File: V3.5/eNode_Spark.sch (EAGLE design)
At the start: 80 parts, among them Q1 MOSFET-PCHANNEL_SOT23-3, U1 WM-N-BM-09, U10 OPA344, U2 MCP73831T-2ACI/OT, U3 R8008-33, U5 HTU21DSMD, U6 TMP006, U7 BMP180, U8 USD-SOCKETSMD, U9 MIC9.7MM

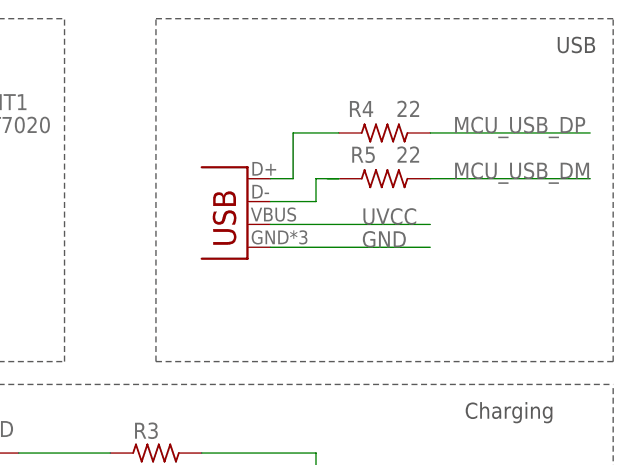
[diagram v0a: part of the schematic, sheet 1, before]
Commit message: Changed to Micro USB B.lbr
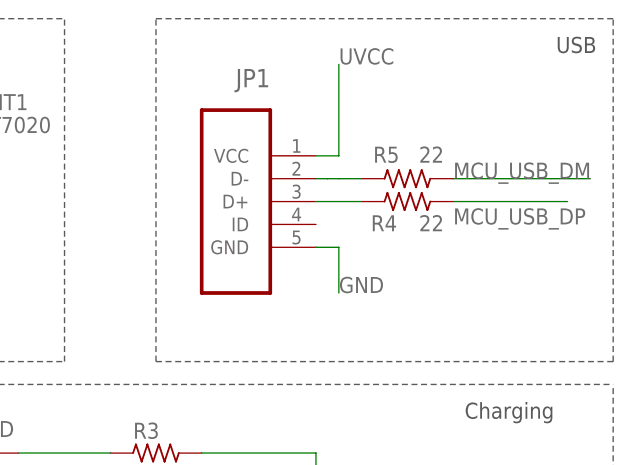
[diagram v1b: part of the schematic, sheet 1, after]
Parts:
- JP1: value USBUSB-MICROB-SLOT-HOLE -> (none); device Spark:USBUSB-MICROB-SLOT-HOLE -> Micro USB B:47346-0001
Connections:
- net MF renamed N$17
- net UVCC: now also JP1.VCC; no longer JP1.VBUS
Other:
- moved on the sheet: R4, R5
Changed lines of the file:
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@@
 <part name="+3V21" library="supply1" deviceset="+3V3" device=""/>
 <part name="R20" library="rc-master-smd" deviceset="R_" device="0603" value="2K"/>
-<part name="JP1" library="Spark" deviceset="USB" device="USB-MICROB-SLOT-HOLE"/>
+<part name="JP1" library="Micro USB B" deviceset="47346-0001" device=""/>
 </parts>
 <sheets>
@@
 <instance part="SW" gate="G$1" x="167.64" y="50.8" rot="MR0"/>
 <instance part="U$5" gate="G$1" x="0" y="0"/>
-<instance part="R4" gate="G$1" x="231.14" y="154.94" smashed="yes" rot="R180">
-<attribute name="NAME" x="227.076" y="156.718" size="1.778" layer="95"/>
-<attribute name="VALUE" x="232.41" y="156.718" size="1.778" layer="96"/>
-</instance>
-<instance part="R5" gate="G$1" x="231.14" y="149.86" smashed="yes" rot="R180">
-<attribute name="NAME" x="227.33" y="151.638" size="1.778" layer="95"/>
-<attribute name="VALUE" x="232.41" y="151.638" size="1.778" layer="96"/>
+<instance part="R4" gate="G$1" x="233.68" y="147.32" smashed="yes" rot="R180">
+<attribute name="NAME" x="229.616" y="144.018" size="1.778" layer="95"/>
+<attribute name="VALUE" x="234.95" y="144.018" size="1.778" layer="96"/>
+</instance>
+<instance part="R5" gate="G$1" x="233.68" y="149.86" smashed="yes" rot="R180">
+<attribute name="NAME" x="229.87" y="151.638" size="1.778" layer="95"/>
+<attribute name="VALUE" x="234.95" y="151.638" size="1.778" layer="96"/>
 </instance>
 <instance part="U1" gate="G$1" x="81.28" y="78.74"/>
@@
 <attribute name="VALUE" x="193.04" y="58.42" size="1.778" layer="96"/>
 </instance>
-<instance part="JP1" gate="G$1" x="215.9" y="142.24" rot="MR0"/>
+<instance part="JP1" gate="G$1" x="213.36" y="147.32" rot="MR0"/>
 </instances>
 <busses>
@@
 <segment>
 <pinref part="JP1" gate="G$1" pin="GND"/>
-<wire x1="218.44" y1="142.24" x2="236.22" y2="142.24" width="0.1524" layer="91"/>
-<label x="228.6" y="142.24" size="1.778" layer="95"/>
+<wire x1="223.52" y1="142.24" x2="226.06" y2="142.24" width="0.1524" layer="91"/>
+<wire x1="226.06" y1="142.24" x2="226.06" y2="137.16" width="0.1524" layer="91"/>
+<label x="226.06" y="137.16" size="1.778" layer="95"/>
 </segment>
 </net>
@@
 </segment>
 <segment>
-<pinref part="JP1" gate="G$1" pin="VBUS"/>
-<wire x1="218.44" y1="144.78" x2="236.22" y2="144.78" width="0.1524" layer="91"/>
-<label x="228.6" y="144.78" size="1.778" layer="95"/>
+<pinref part="JP1" gate="G$1" pin="VCC"/>
+<wire x1="223.52" y1="152.4" x2="226.06" y2="152.4" width="0.1524" layer="91"/>
+<wire x1="226.06" y1="152.4" x2="226.06" y2="162.56" width="0.1524" layer="91"/>
+<label x="226.06" y="162.56" size="1.778" layer="95"/>
 </segment>
 </net>
@@
 <wire x1="224.79" y1="149.86" x2="226.06" y2="149.86" width="0.1524" layer="91"/>
 <pinref part="R5" gate="G$1" pin="2"/>
-<wire x1="226.06" y1="149.86" x2="223.52" y2="149.86" width="0.1524" layer="91"/>
 <pinref part="JP1" gate="G$1" pin="D-"/>
-<wire x1="218.44" y1="147.32" x2="223.52" y2="147.32" width="0.1524" layer="91"/>
-<wire x1="223.52" y1="147.32" x2="223.52" y2="149.86" width="0.1524" layer="91"/>
-</segment>
-</net>
-<net name="MF" class="0">
-<segment>
-<pinref part="R4" gate="G$1" pin="2"/>
-<pinref part="JP1" gate="G$1" pin="D+"/>
-<wire x1="218.44" y1="149.86" x2="220.98" y2="149.86" width="0.1524" layer="91"/>
-<wire x1="220.98" y1="149.86" x2="220.98" y2="154.94" width="0.1524" layer="91"/>
-<wire x1="220.98" y1="154.94" x2="226.06" y2="154.94" width="0.1524" layer="91"/>
+<wire x1="226.06" y1="149.86" x2="228.6" y2="149.86" width="0.1524" layer="91"/>
+<wire x1="224.79" y1="149.86" x2="223.52" y2="149.86" width="0.1524" layer="91"/>
 </segment>
 </net>
 <net name="MCU_USB_DP" class="0">
 <segment>
-<wire x1="236.22" y1="154.94" x2="254" y2="154.94" width="0.1524" layer="91"/>
-<label x="238.76" y="154.94" size="1.778" layer="95"/>
+<wire x1="238.76" y1="147.32" x2="251.46" y2="147.32" width="0.1524" layer="91"/>
+<label x="238.76" y="144.78" size="1.778" layer="95"/>
 <pinref part="R4" gate="G$1" pin="1"/>
 </segment>
@@
 <net name="MCU_USB_DM" class="0">
 <segment>
-<wire x1="236.22" y1="149.86" x2="254" y2="149.86" width="0.1524" layer="91"/>
+<wire x1="238.76" y1="149.86" x2="254" y2="149.86" width="0.1524" layer="91"/>
 <label x="238.76" y="149.86" size="1.778" layer="95"/>
 <pinref part="R5" gate="G$1" pin="1"/>
@@
 <wire x1="43.18" y1="78.74" x2="22.86" y2="78.74" width="0.1524" layer="91"/>
 <label x="22.86" y="78.74" size="1.778" layer="95"/>
+</segment>
+</net>
+<net name="N$17" class="0">
+<segment>
+<pinref part="JP1" gate="G$1" pin="D+"/>
+<pinref part="R4" gate="G$1" pin="2"/>
+<wire x1="223.52" y1="147.32" x2="228.6" y2="147.32" width="0.1524" layer="91"/>
 </segment>
 </net>
@@
 </segment>
 </net>
-<net name="N$13" class="0">
+<net name="N$25" class="0">
 <segment>
 <pinref part="U6" gate="G$1" pin="!DRDY"/>
@@
 </sheet>
 </sheets>
+<errors>
+</errors>
 </schematic>
 </drawing>
